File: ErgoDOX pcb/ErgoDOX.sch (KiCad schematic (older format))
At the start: 63 parts, among them J1 USB, J2 3.5mm, J3 JMP, J4 JMP, SW0:10 SW0:3, SW0:11 SW0:2, SW0:12 SW0:1, SW0:7 SW0:6, SW0:8 SW0:5, SW0:9 SW0:4, SW1:10 SW1:3, SW1:11 SW1:2, SW1:12 SW1:1, SW1:13 SW1:0, SW1:9 SW1:4, SW2:10 SW2:3, SW2:11 SW2:2, SW2:12 SW2:1, SW2:13 SW2:0, SW2:7 SW2:6, SW2:8 SW2:5, SW2:9 SW2:4, SW3:10 SW3:3, SW3:11 SW3:2, SW3:12 SW3:1, SW3:13 SW3:0, SW3:8 SW3:5, SW3:9 SW3:4, SW4:10 SW4:3, SW4:11 SW4:2, SW4:12 SW4:1, SW4:13 SW4:0, SW4:7 SW4:6, SW4:8 SW4:5, SW4:9 SW4:4, SW5:10 SW5:3, SW5:11 SW5:2, SW5:12 SW5:1, SW5:13 SW5:0, SW5:7 SW5:6, SW5:8 SW5:5, SW5:9 SW5:4, U1 TEENSY2.0, U2 MCP23018

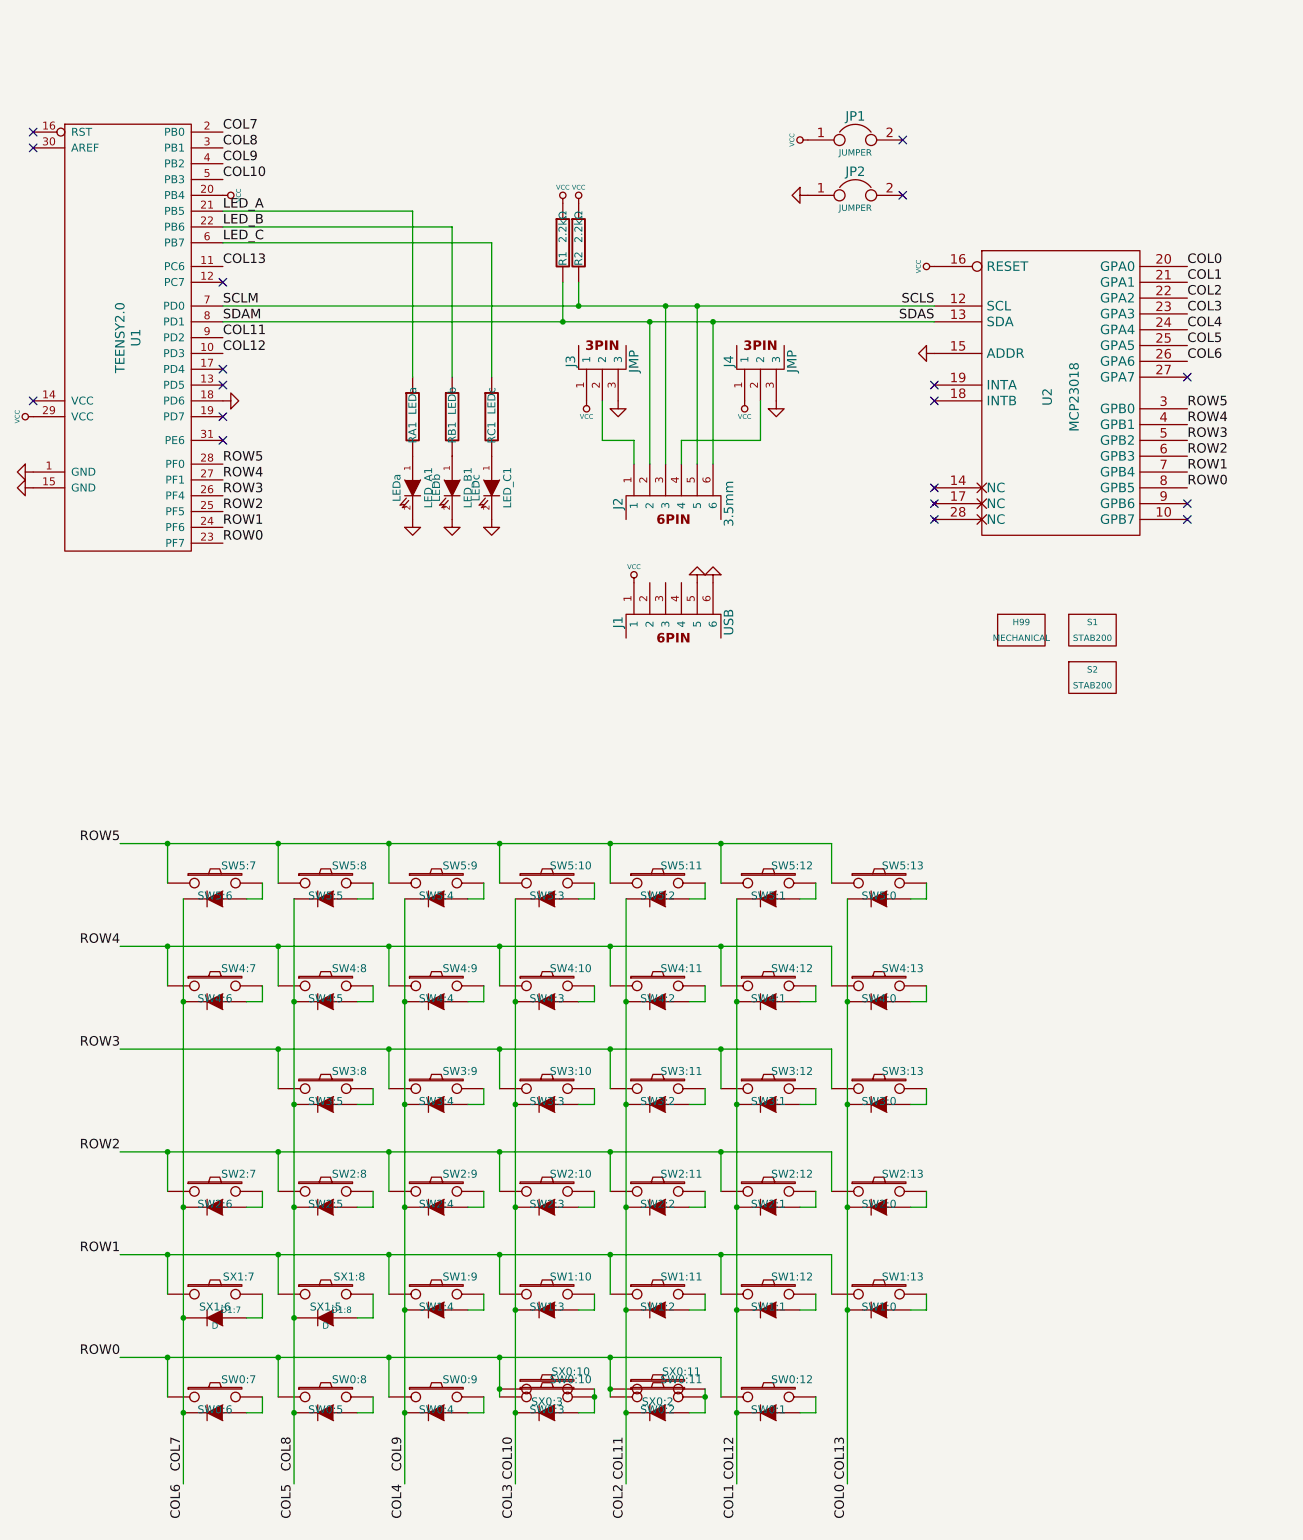
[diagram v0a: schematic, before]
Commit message: Adding support for reversible female USB Port and optional reset switch. This will allow the right hand of the Ergodox to be flipped and used as the left hand. In this scenario the teensy should be soldered with its bottom facing up on the top of the left hand PCB. Because doing this obscures the teensy mounted reset button, I have added pads for an optional reset switch that can be used from the bottom of a left hand only Ergodox.
Reset switch part number: OMRON B3U-1000P
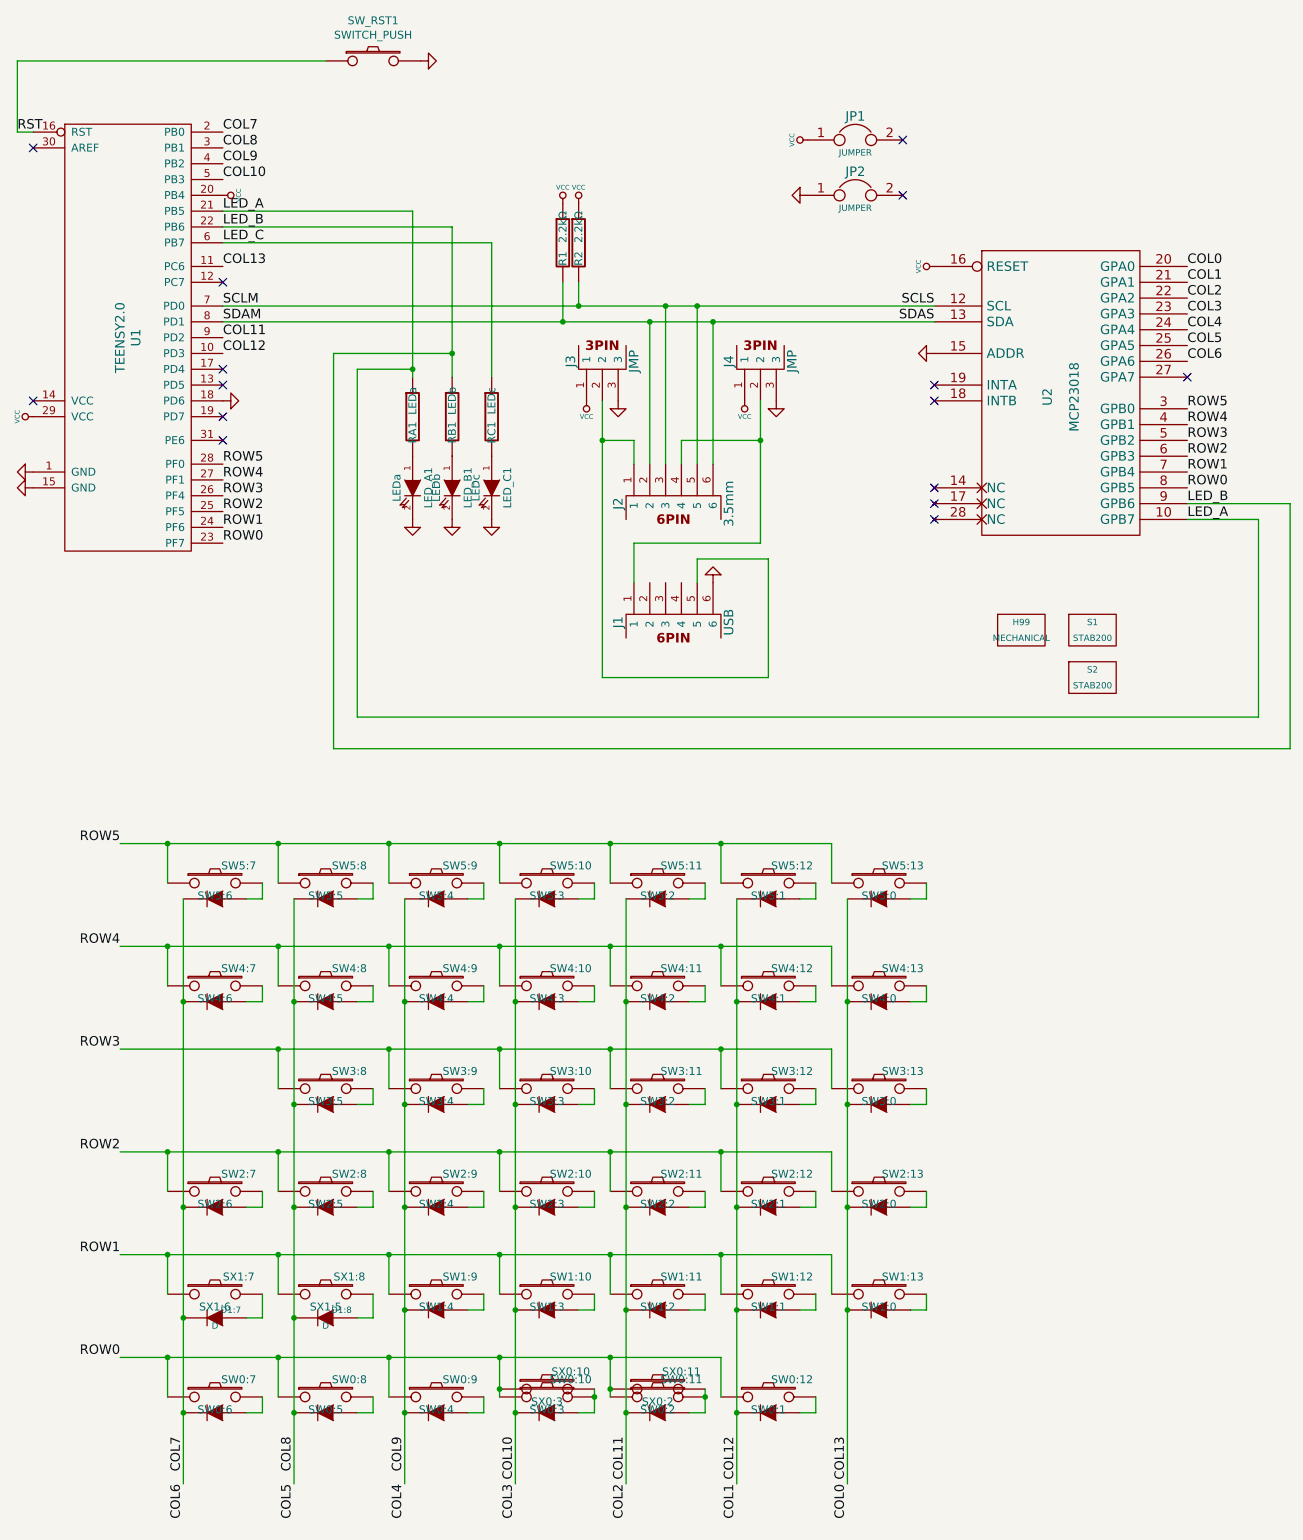
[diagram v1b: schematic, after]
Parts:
- added SW_RST1: SWITCH_PUSH, Buttons_Switches_SMD:SW_SPST_B3U-1000P, symbol SWITCH_PUSH
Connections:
- net GND: now also SW_RST1.0 (GND), SW_RST1.2; no longer J1.5
- net LED_A: now also U2.10 (GPB7)
- net LED_B: now also U2.9 (GPB6)
- net VCC: no longer J1.1
- net at J2.1, J3.2: now also J1.5
- net at J2.4, J4.2: now also J1.1
- net RST: now reaches U1.16 (RST)
- net RST: now also SW_RST1.1
- no-connect marks 18 -> 15
